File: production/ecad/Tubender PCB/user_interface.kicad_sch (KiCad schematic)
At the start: 75 parts, among them IC1 74HC4050D, IC2 RA8875L3N, IC3 SN74LVC1G29DCTR, J12 640387-2, J15 640387-2, J16 640387-2, J17 640387-2, J18 640387-2, J19 640387-2, J20 640387-2, J21 640387-2, J22 640387-2, J23 640387-2, J24 640387-2, J25 640387-2, J26 640387-2, J27 640387-2, J28 640387-2, J29 640387-5, J7 4-1734592-0, U11 SN74AHC1G125DBVR, U5 74HC595, U6 PEC11R-4215K-S0024, U8 CD4051BE, U9 CD4051BE, Y1 ABM8-20.000MHz-10-B1U-T

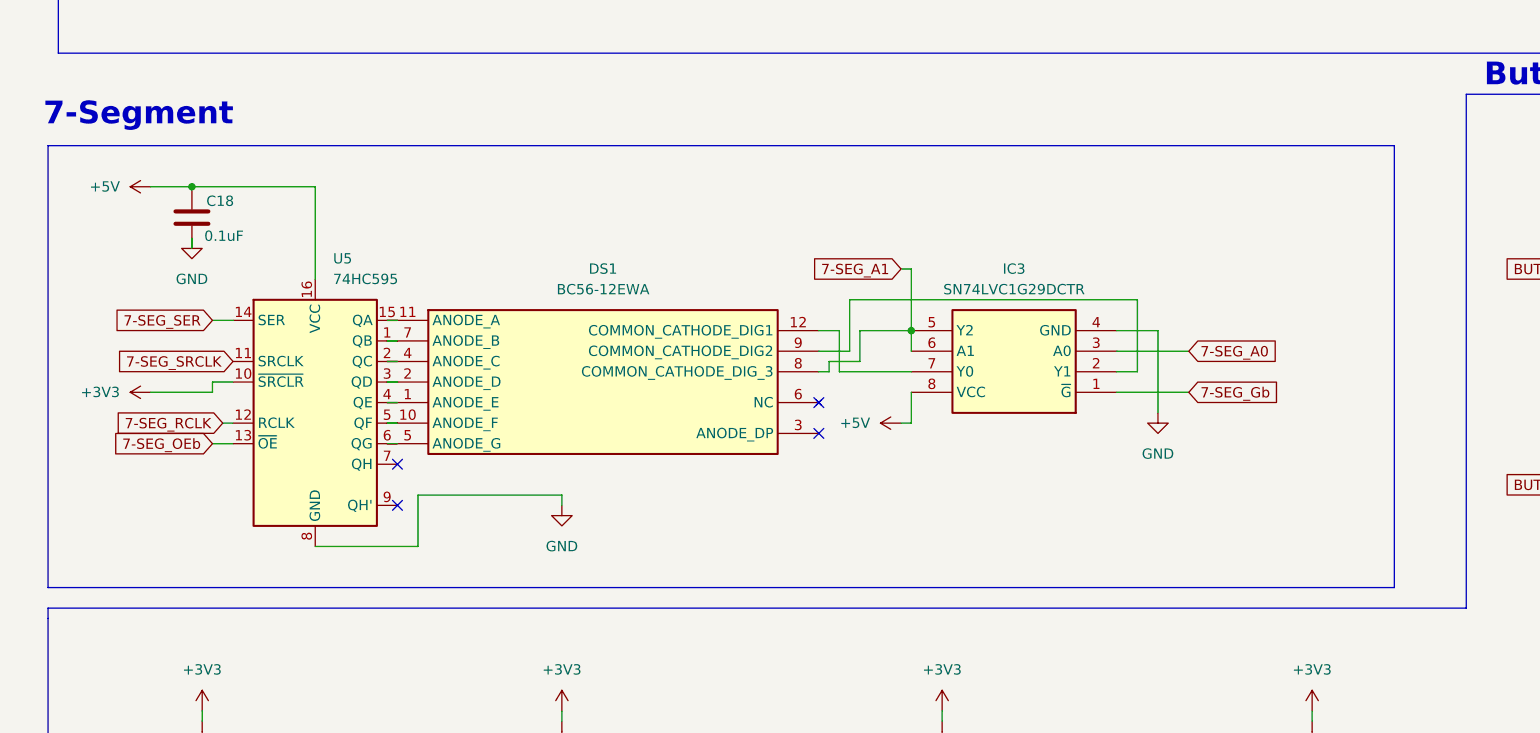
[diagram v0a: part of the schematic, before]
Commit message: Replace outdated shift register
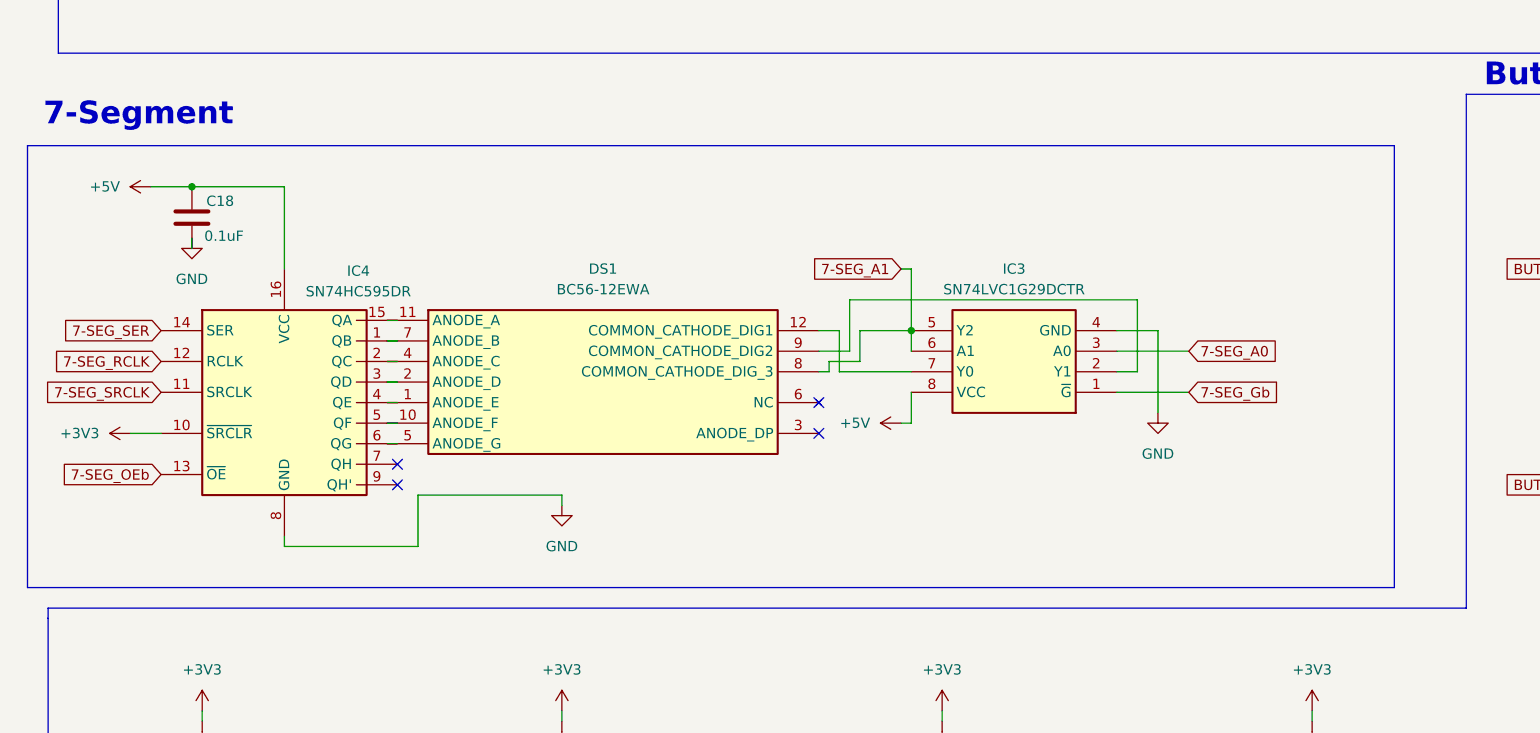
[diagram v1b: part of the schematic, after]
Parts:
- removed U5: 74HC595, symbol 74xx:74HC595
- added IC4: SN74HC595DR, SOIC127P600X175-16N, symbol SamacSys_Parts:SN74HC595DR
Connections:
- net +3V3: now also IC4.10 (~{SRCLR})
- net +5V: now also IC4.16 (VCC)
- net 7-SEG_OEb: now also IC4.13 (~{OE})
- net 7-SEG_RCLK: now also IC4.12 (RCLK)
- net 7-SEG_SER: now also IC4.14 (SER)
- net 7-SEG_SRCLK: now also IC4.11 (SRCLK)
- net GND: now also IC4.8 (GND)
- net at DS1.7 (ANODE_B): now also IC4.1 (QB)
- net at DS1.11 (ANODE_A): now also IC4.15 (QA)
- net at DS1.4 (ANODE_C): now also IC4.2 (QC)
- net at DS1.2 (ANODE_D): now also IC4.3 (QD)
- net at DS1.1 (ANODE_E): now also IC4.4 (QE)
- net at DS1.10 (ANODE_F): now also IC4.5 (QF)
- net at DS1.5 (ANODE_G): now also IC4.6 (QG)

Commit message: UI Board Fully Separated Now
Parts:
- removed C10, C11: 0.01u, symbol Device:C_Small
- removed C18: 0.1uF, symbol Device:C
- removed DS1: BC56-12EWA, DIPS1524W50P254L3760H835Q12N, symbol SamacSys_Parts:BC56-12EWA
- removed IC3: SN74LVC1G29DCTR, SOP65P400X130-8N, symbol SamacSys_Parts:SN74LVC1G29DCTR
- removed IC4: SN74HC595DR, SOIC127P600X175-16N, symbol SamacSys_Parts:SN74HC595DR
- removed J29: 640387-5, 640387-5:TE_640387-5, symbol 640387-5:640387-5
- removed R20, R22: 10k, symbol Device:R_Small_US
- removed U6: PEC11R-4215K-S0024, PEC11R-4XXXK-SXXXX, symbol SamacSys_Parts:PEC11R-4215K-S0024
- added C19, C20, C21, C22, C23, C24, C25, C26, C27, C28, C29, C30, C31, C32, C33: 500nF, symbol Device:C_Small
- added J29: 1-640387-0, 1-640387-0:TE_1-640387-0, symbol 1-640387-0:1-640387-0
- added J31: 640387-5, 640387-5:TE_640387-5, symbol 640387-5:640387-5
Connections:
- net +3V3: now also J12.1, J15.1, J16.1, J17.1, J18.1, J19.1, J20.1, J21.1, J22.1, J23.1, J24.1, J25.1, J26.1, J27.1, J28.1, J29.2; no longer R49.2, R50.2, R51.2, R52.2, R53.2, R54.2, R55.2, R56.2, R57.2, R58.2, R59.2, R60.2, R61.2, R62.2, R63.2
- net +5V: now also J29.1, J31.1
- net 7-SEG_A0: now also J29.7
- net 7-SEG_A1: now also J29.8
- net 7-SEG_Gb: now also J29.9
- net 7-SEG_OEb: now also J29.5
- net 7-SEG_RCLK: now also J29.4
- net 7-SEG_SER: now also J29.6
- net 7-SEG_SRCLK: now also J29.3
- net BUTTON_0: now also J20.2, R55.2, C26.1; no longer J12.1, R49.1
- net BUTTON_1: now also J23.2, R58.2, C28.1; no longer J15.1, R50.1
- net BUTTON_10: now also J15.2, R50.2, C21.1; no longer J24.1, R59.1
- net BUTTON_11: now also J16.2, R51.2, C22.1
- net BUTTON_12: now also J17.2, R52.2, C23.1; no longer J26.1, R61.1
- net BUTTON_13: now also J18.2, R53.2, C24.1; no longer J27.1, R62.1
- net BUTTON_14: now also J27.2, R62.2, C32.1; no longer J28.1, R63.1
- net BUTTON_2: now also J25.2, R60.2, C30.1; no longer J16.1, R51.1
- net BUTTON_3: now also J19.2, R54.2, C25.1; no longer J17.1, R52.1
- net BUTTON_4: now also J21.2, R56.2, C27.1; no longer J18.1, R53.1
- net BUTTON_5: now also J24.2, R59.2, C29.1; no longer J19.1, R54.1
- net BUTTON_6: now also J26.2, R61.2, C31.1; no longer J21.1, R56.1
- net BUTTON_7: now also J28.2, R63.2, C33.1; no longer J20.1, R55.1
- net BUTTON_8: now also J22.2, R57.2, C19.1; no longer J22.1, R57.1
- net BUTTON_9: now also J12.2, R49.2, C20.1; no longer J23.1, R58.1
- net DIAL_BUTTON: now also J31.2
- net DIAL_CHANNEL_A: now also J31.4
- net DIAL_CHANNEL_B: now also J31.3
- net GND: now also R49.1, R50.1, R51.1, R52.1, R53.1, R54.1, R55.1, R56.1, R57.1, R58.1, R59.1, R60.1, R61.1, R62.1, R63.1, C19.2, C20.2, C21.2, C22.2, C23.2, C24.2, C25.2, C26.2, C27.2, C28.2, C29.2, C30.2, C31.2, C32.2, C33.2, J29.10, J31.5; no longer J12.2, J15.2, J16.2, J17.2, J18.2, J19.2, J20.2, J21.2, J22.2, J23.2, J24.2, J25.2, J26.2, J27.2, J28.2
- no-connect marks 51 -> 47
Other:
- note added: "7 Segment Connector"
- note added: "Rotary Connector"
- note removed: "7-Segment"
- note removed: "Rotary Encoder"
- moved on the sheet: J22

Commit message: start power layout
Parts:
- C12, C13, C14, C15, C16, C17, C19, C20, C21, C22, C23, C24, C25, C26, C27, C28, C29, C30, C31, C32, C33: footprint (none) -> Capacitor_SMD:C_0805_2012Metric
- J12, J15, J16, J17, J18, J19, J20, J21, J22, J23, J24, J25, J26, J27, J28: footprint 640387-2:TE_640387-2 -> ${KIPRJMOD}:TE_640387-2
- J29: footprint 1-640387-0:TE_1-640387-0 -> ${KIPRJMOD}:TE_1-640387-0
- J31: footprint 640387-5:TE_640387-5 -> ${KIPRJMOD}:TE_640387-5
- R21, R23, R24, R25, R26, R27, R28, R29, R30, R31, R32, R33, R34, R35, R36, R37, R38, R39, R40, R41, R42, R43, R49, R50, R51, R52, R53, R54, R55, R56, R57, R58, R59, R60, R61, R62, R63: footprint (none) -> Resistor_SMD:R_0805_2012Metric
- U11: footprint SN74AHC1G125DBVR:SOT95P280X145-5N -> ${KIPRJMOD}:SOT95P280X145-5N
- U8, U9: footprint CD4051BE:DIP794W45P254L1969H508Q16 -> ${KIPRJMOD}:DIP794W45P254L1969H508Q16
- Y1: footprint ABM8-20.000MHz-10-B1U-T:XTAL_ABM8-20.000MHz-10-B1U-T -> ${KIPRJMOD}:XTAL_ABM8-20.000MHz-10-B1U-T

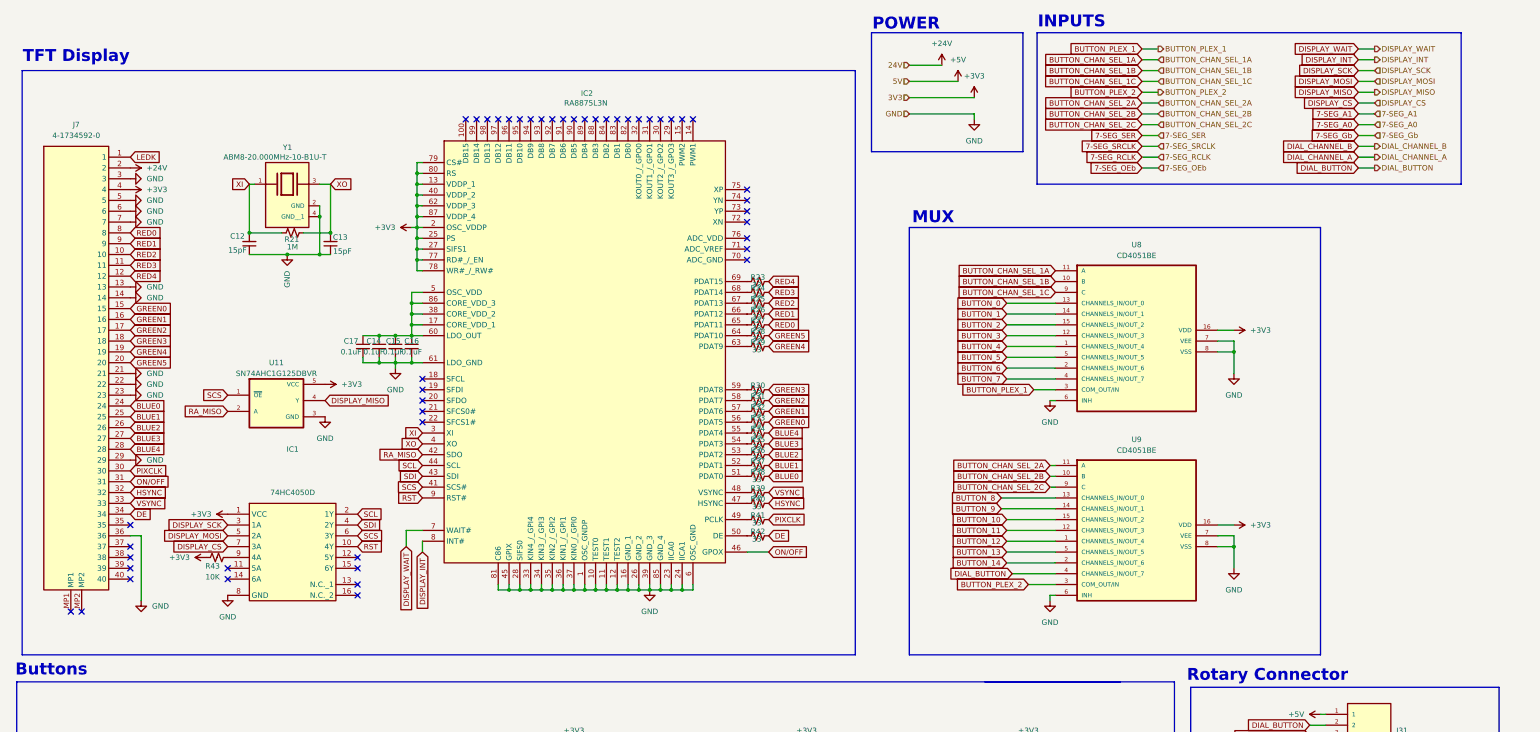
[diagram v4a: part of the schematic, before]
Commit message: Replaced MUX IC and connected touch functionality pins
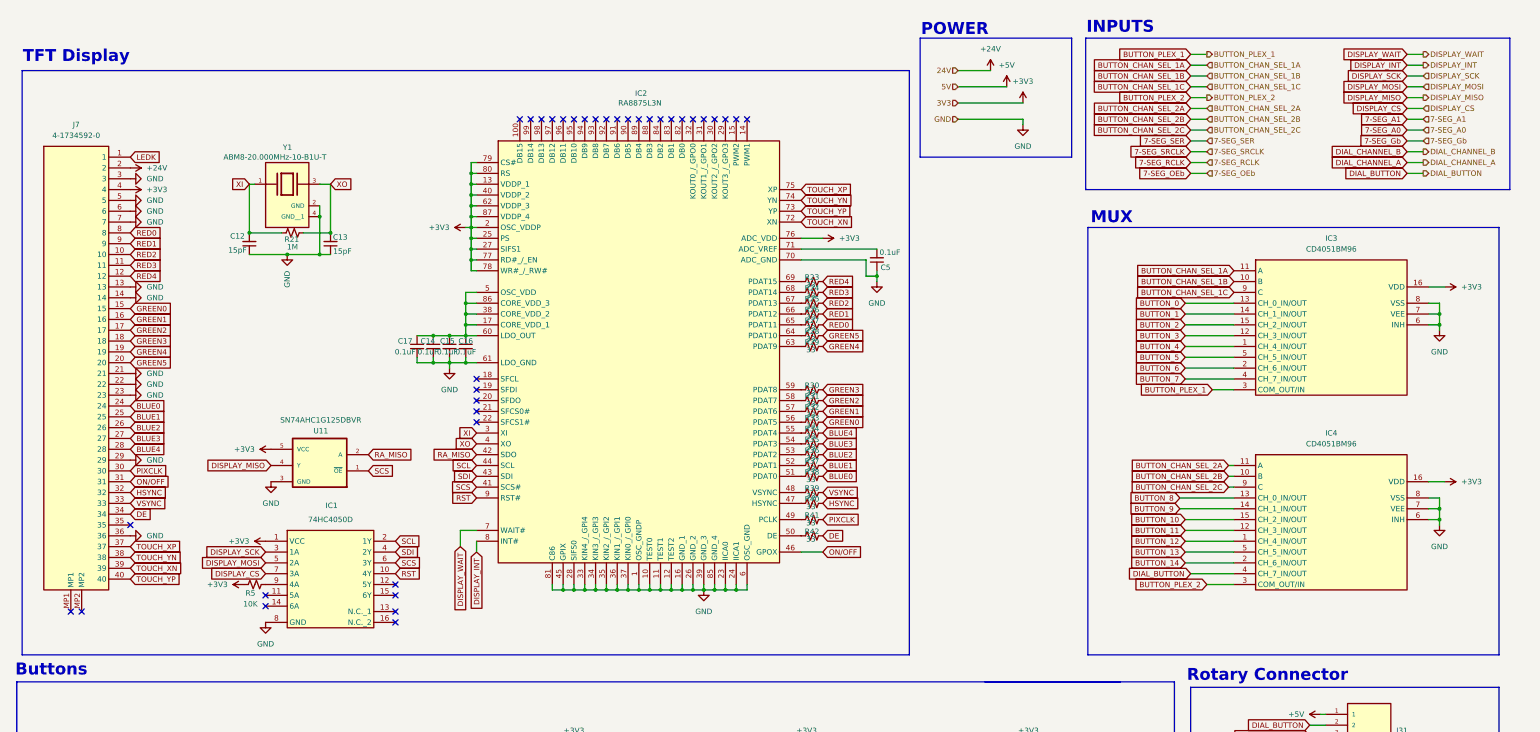
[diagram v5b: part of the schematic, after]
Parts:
- removed R43: 10K, Resistor_SMD:R_0805_2012Metric, symbol Device:R_Small_US
- removed U8, U9: CD4051BE, ${KIPRJMOD}:DIP794W45P254L1969H508Q16, symbol CD4051BE:CD4051BE
- added C5: 0.1uF, Capacitor_SMD:C_0805_2012Metric, symbol Device:C_Small
- added IC3, IC4: CD4051BM96, SOIC127P600X175-16N, symbol SamacSys_Parts:CD4051BM96
- added R5: 10K, Resistor_SMD:R_0805_2012Metric, symbol Device:R_Small_US
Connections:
- net +3V3: now also IC2.76 (ADC_VDD), IC3.16 (VDD), IC4.16 (VDD), R5.2
- net BUTTON_0: now also IC3.13 (CH_0_IN/OUT)
- net BUTTON_1: now also IC3.14 (CH_1_IN/OUT)
- net BUTTON_10: now also IC4.15 (CH_2_IN/OUT)
- net BUTTON_11: now also IC4.12 (CH_3_IN/OUT)
- net BUTTON_12: now also IC4.1 (CH_4_IN/OUT)
- net BUTTON_13: now also IC4.5 (CH_5_IN/OUT)
- net BUTTON_14: now also IC4.2 (CH_6_IN/OUT)
- net BUTTON_2: now also IC3.15 (CH_2_IN/OUT)
- net BUTTON_3: now also IC3.12 (CH_3_IN/OUT)
- net BUTTON_4: now also IC3.1 (CH_4_IN/OUT)
- net BUTTON_5: now also IC3.5 (CH_5_IN/OUT)
- net BUTTON_6: now also IC3.2 (CH_6_IN/OUT)
- net BUTTON_7: now also IC3.4 (CH_7_IN/OUT)
- net BUTTON_8: now also IC4.13 (CH_0_IN/OUT)
- net BUTTON_9: now also IC4.14 (CH_1_IN/OUT)
- net BUTTON_CHAN_SEL_1A: now also IC3.11 (A)
- net BUTTON_CHAN_SEL_1B: now also IC3.10 (B)
- net BUTTON_CHAN_SEL_1C: now also IC3.9 (C)
- net BUTTON_CHAN_SEL_2A: now also IC4.11 (A)
- net BUTTON_CHAN_SEL_2B: now also IC4.10 (B)
- net BUTTON_CHAN_SEL_2C: now also IC4.9 (C)
- net BUTTON_PLEX_1: now also IC3.3 (COM_OUT/IN)
- net BUTTON_PLEX_2: now also IC4.3 (COM_OUT/IN)
- net DIAL_BUTTON: now also IC4.4 (CH_7_IN/OUT)
- net GND: now also IC2.70 (ADC_GND), C5.1, IC3.6 (INH), IC3.7 (VEE), IC3.8 (VSS), IC4.6 (INH), IC4.7 (VEE), IC4.8 (VSS)
- net at IC2.71 (ADC_VREF): now also C5.2
- net TOUCH_XN: now reaches IC2.72 (XN)
- net TOUCH_XN: now also J7.39
- net TOUCH_YP: now reaches IC2.73 (YP)
- net TOUCH_YP: now also J7.40
- net TOUCH_YN: now reaches IC2.74 (YN)
- net TOUCH_YN: now also J7.38
- net TOUCH_XP: now reaches IC2.75 (XP)
- net TOUCH_XP: now also J7.37
- net at IC1.9 (4A): now also R5.1
- no-connect marks 47 -> 36
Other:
- moved on the sheet: C14, C15, C16, C17, IC2, R23, R24, R25, R26, R27, R28, R29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

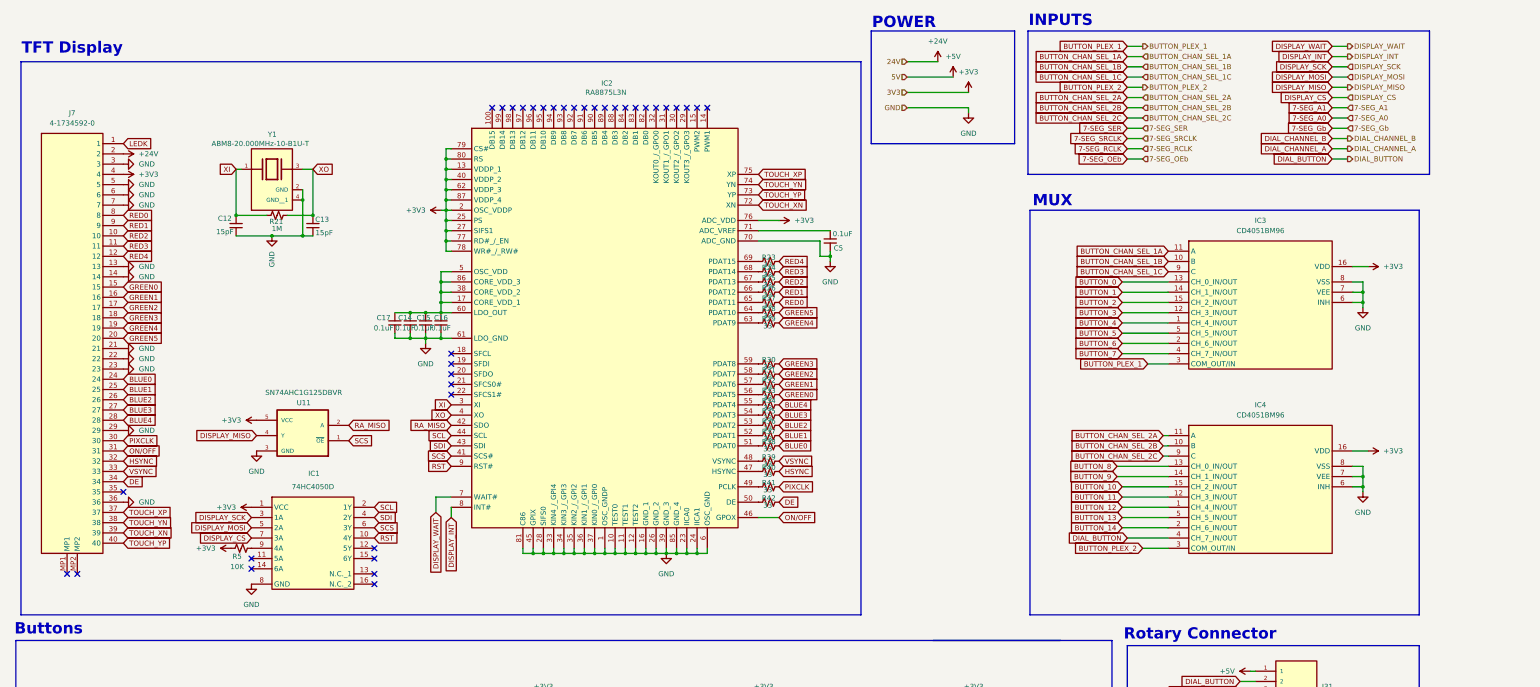
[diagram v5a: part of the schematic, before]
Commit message: Added Testpoints to UI sheet
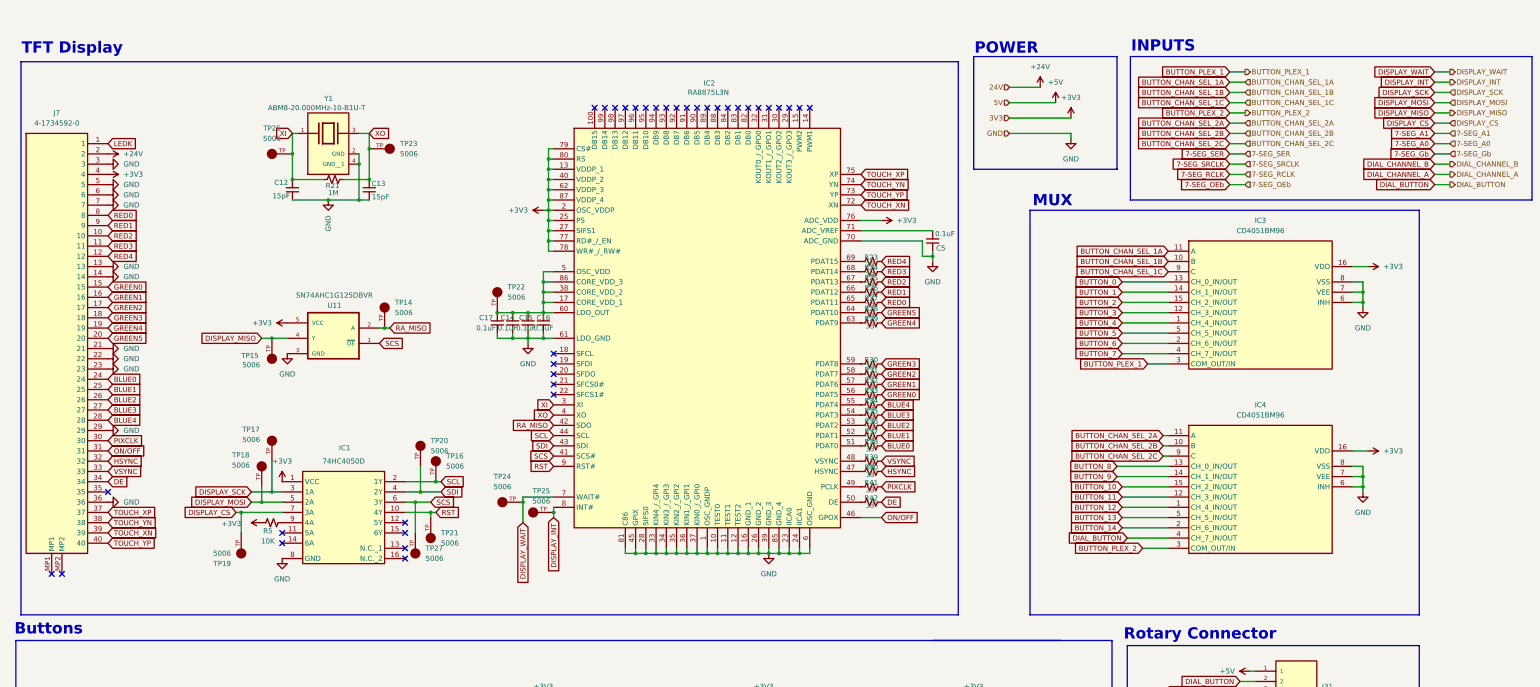
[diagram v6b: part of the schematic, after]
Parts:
- added TP14, TP15, TP16, TP17, TP18, TP19, TP20, TP21, TP22, TP23, TP24, TP25, TP26, TP27: 5006, 5006:KEYSTONE_5006, symbol 5006:5006
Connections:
- net DISPLAY_CS: now also TP19.TP
- net DISPLAY_INT: now also TP25.TP
- net DISPLAY_MISO: now also TP15.TP
- net DISPLAY_MOSI: now also TP18.TP
- net DISPLAY_SCK: now also TP17.TP
- net DISPLAY_WAIT: now also TP24.TP
- net RA_MISO: now also TP14.TP
- net RST: now also TP21.TP
- net SCL: now also TP16.TP
- net SCS: now also TP27.TP
- net SDI: now also TP20.TP
- net XI: now also TP26.TP
- net XO: now also TP23.TP
- net at C14.1, C15.1, C16.1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: now also TP22.TP
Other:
- moved on the sheet: C12, C13, C14, C15, C16, C17, C5, IC1, IC2, J7, R21, R23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

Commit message: Added Footprints
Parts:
- IC1: footprint SOIC127P600X175-16N -> footprints:SOT109-1_NXP
- IC2: footprint QFP50P1600X1600X160-100N -> footprints:QFP40P1600X1600X160-128N
- IC3, IC4: footprint SOIC127P600X175-16N -> footprints:SOIC127P600X175-16N
- J7: footprint 417345920 -> footprints:TE_4-1734592-0
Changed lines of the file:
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@@
 			)
 		)
-		(property "Footprint" "SOIC127P600X175-16N"
+		(property "Footprint" "footprints:SOIC127P600X175-16N"
 			(at 353.06 216.84 0)
 			(effects
@@
 			)
 		)
-		(property "Footprint" "SOIC127P600X175-16N"
+		(property "Footprint" "footprints:SOT109-1_NXP"
 			(at 118.11 228.27 0)
 			(effects
@@
 			)
 		)
-		(property "Footprint" "QFP50P1600X1600X160-100N"
+		(property "Footprint" "footprints:QFP40P1600X1600X160-128N"
 			(at 231.14 143.18 0)
 			(effects
@@
 			)
 		)
-		(property "Footprint" "417345920"
+		(property "Footprint" "footprints:TE_4-1734592-0"
 			(at 44.45 144.45 0)
 			(effects
@@
 			)
 		)
-		(property "Footprint" "SOIC127P600X175-16N"
+		(property "Footprint" "footprints:SOIC127P600X175-16N"
 			(at 353.06 171.12 0)
 			(effects
